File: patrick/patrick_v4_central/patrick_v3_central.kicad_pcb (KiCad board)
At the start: 2 copper layers, 53.1 x 53.9 mm, 14 parts, among them J1 Conn_02x05_Counter_Clockwise, J10 61300311121, J2 Conn_02x05_Counter_Clockwise, J3 Conn_02x05_Counter_Clockwise, J4 Conn_02x05_Counter_Clockwise, J5 Conn_02x05_Counter_Clockwise, J7 61300211121, J9 61300211121, U3 BL652-SA-01

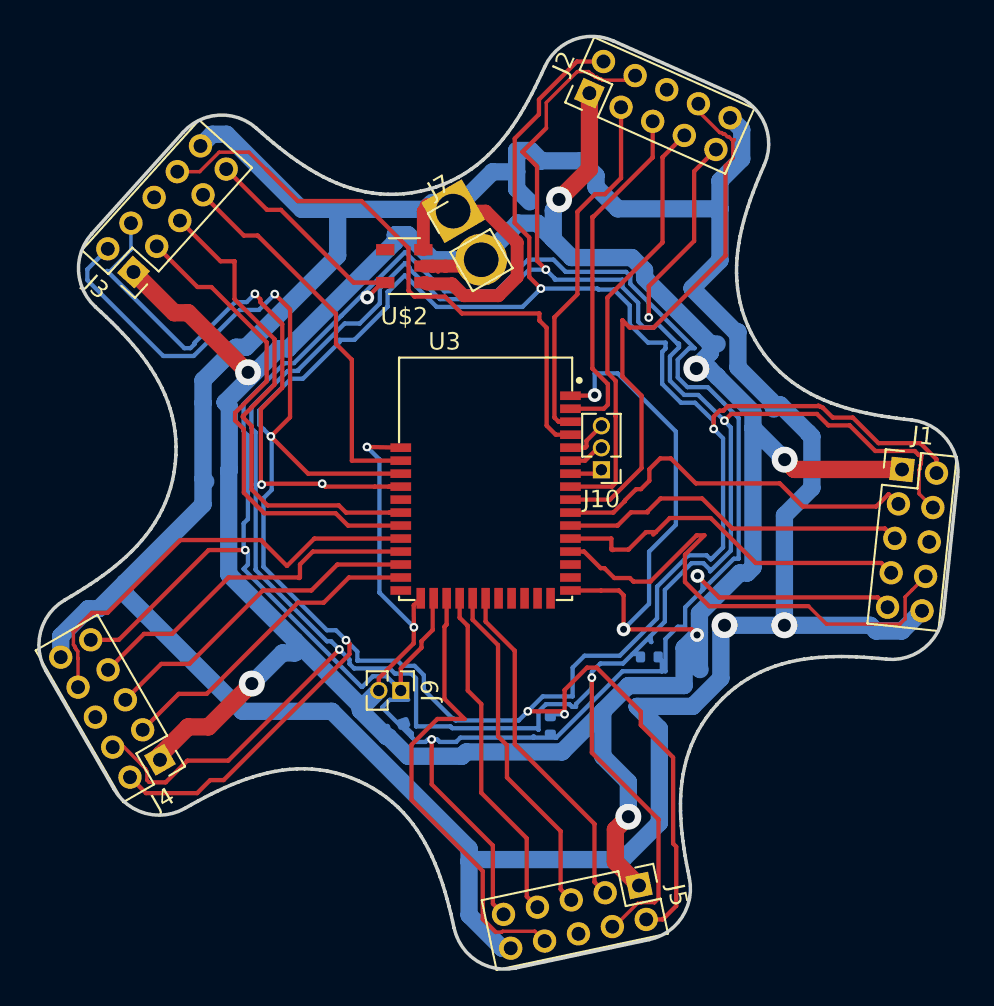
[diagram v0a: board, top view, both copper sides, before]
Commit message: added IMU to 3 legged circuit
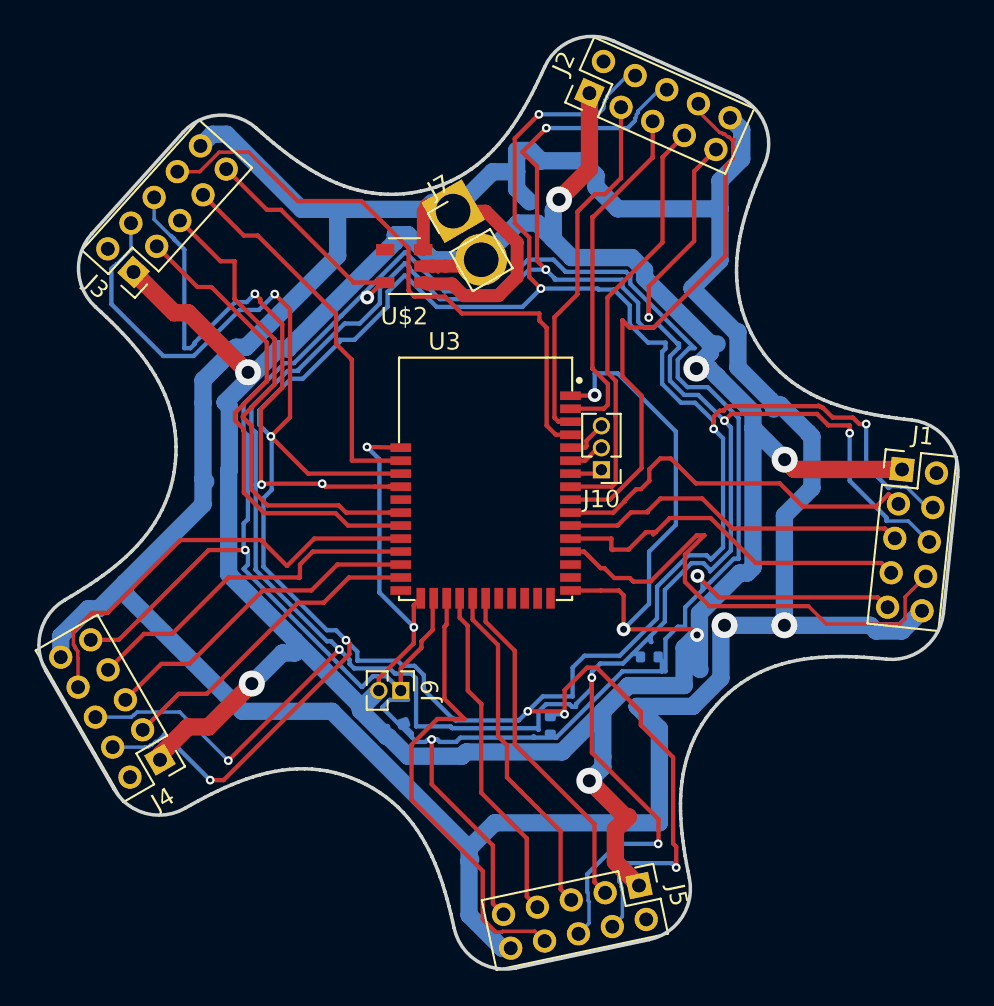
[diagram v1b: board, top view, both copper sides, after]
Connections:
- J1 pad 2: /SDA -> Net-(J1-Pad2)
- J1 pad 4: /SCL -> /SDA
- J1 pad 6: Net-(J1-Pad6) -> /SCL
- J2 pad 2: /SDA -> Net-(J2-Pad2)
- J2 pad 4: /SCL -> /SDA
- J2 pad 6: Net-(J2-Pad6) -> /SCL
- J3 pad 2: /SDA -> Net-(J3-Pad2)
- J3 pad 4: /SCL -> /SDA
- J3 pad 6: Net-(J3-Pad6) -> /SCL
- J4 pad 2: /SDA -> Net-(J4-Pad2)
- J4 pad 4: /SCL -> /SDA
- J4 pad 6: Net-(J4-Pad6) -> /SCL
- J5 pad 2: /SDA -> Net-(J5-Pad2)
- J5 pad 4: /SCL -> /SDA
- J5 pad 6: Net-(J5-Pad6) -> /SCL
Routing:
- net /SDA: track 199.7 -> 208.3 mm, vias 7 -> 11
- net /SCL: track 203.6 -> 206.6 mm, vias 7 -> 11
- net GND: track 213.5 -> 214.3 mm
